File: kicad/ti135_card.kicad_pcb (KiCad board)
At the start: 8 copper layers, 76 x 65.1 mm, 302 parts, among them J1 JTAG 3.3V, J2 UART 3.3V, J3 2x19 1.27mm socket (bottom), J5 LCD 1x14 2.54mm, J6 2x3 1.27mm (bottom), J9 HR911130A, U1001 THGAMVG7T13BAIL, U101 NCP163ASN330T1G, U1201 SN74AXC8T245PWR, U1202 SN74AXC8T245PWR, U1203 SN74AXC8T245PWR, U1204 SN74AXC8T245PWR, U1301 SN74LV4051APWR, U1302 OPA365AIDBVR, U1303 ADS7056IRUGR, U201 TLV62585PDRLR, U301 TLV62585PDRLR, U311 TLV62585PDRLR, U321 TLV62585PDRLR, U331 TLV62585PDRLR, U341 TLV62585PDRLR, U401 TPS3808G01DBVR, U501 Ti135N484I3, U601 IS25WP128-RHLE, U801 H9HCNNN8KUMLHR-NME, U901 KSZ9031RNXCA, U902 74LVC1G06GW, Y701 SiT8924BA-73-18N-25.000000, Y901 25MHz

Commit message: Placement with KiCadRoutingTools; Ethernet PHY changed to RTL8211FDI-CG
- Sheet 09 redone for the RTL8211FDI-CG (C692886; the KSZ9031 had 16 orderable, and the
  Agilex 5 card makes the same change). It runs from 3V3 only, with an internal 1.0 V core LDO
  and RGMII pads at 1.8 V from its pad LDO; all nine straps are fitted. PHYRSTB is a 3.3 V
  input, so it is driven through a 74LVC1G07 open drain. The jack LED is driven straight
  from LED2.
- The 1V2 buck (U321) is removed. Power budget and docs updated.
- make_board sets pad pin functions/types, so the placer reads the Y701 oscillator correctly.
- Placement: placement/ holds the inputs (groups, prep, intent fixes, judging chain). Seed 1
  of 12 was chosen by the quick-route judge and applied with tools/apply_placement.py.
  build_pcb.sh no longer rebuilds by default; --rebuild restores the poses.
- tools/jlc: the jlc-tools submodule.

Co-Authored-By: Claude Opus 5.5 <noreply@anthropic.com>
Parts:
- removed C321: 10u, Capacitor_SMD:C_0805_2012Metric
- removed C322, C923: 22u, Capacitor_SMD:C_0805_2012Metric
- removed C924, C942, C943: 100n, Capacitor_SMD:C_0402_1005Metric
- removed FB902: BLM15PX121SN1D, Inductor_SMD:L_0402_1005Metric
- removed L321: 1u, Inductor_SMD:L_Coilcraft_XxL4020
- removed R321, R322: 100k, Resistor_SMD:R_0402_1005Metric
- removed U321: TLV62585PDRLR, Package_TO_SOT_SMD:SOT-563
- added R932: 10k, Resistor_SMD:R_0402_1005Metric, F.Cu at (191.7, 73.9)
- added R933: 10k, Resistor_SMD:R_0402_1005Metric, F.Cu at (184.7, 72.8)
- C509, C510, C511, C512, C513, C514, C515, C516, C517, C518, C519, C520, C521, C522, C523, C524, C525, C526, C527, C528, C529, C530, C531, C532, C533, C534, C535, C536, C537, C538, C539, C540, C541, C542, C543, C544, C545, C546, C547, C548, C549, C550, C551, C552, C553, C554, C555, C556, C557, C558, C559, C560, C561, C562, C563, C564, C565, C803, C804, C805, C806, C807, C808, C809, C810, C811, C812, C813, C814, C815, C816, C817, C818, C819, C820, C821, C822, C823, C824, C825, C826, C827, C828, C829, C830, C831, C832, C833, C834, C835: moved to B.Cu
- C920: value 22u -> 10u
- C930: value 10u -> 1u; footprint Capacitor_SMD:C_0805_2012Metric -> Capacitor_SMD:C_0402_1005Metric
- C935: value 100n -> 1u
- C940: value 4u7 -> 1u
- R928, R929: value 1k -> 4k7
- R930: value 10k -> 4k7
- R931: value 12.1k 1% -> 2.49k 1%
- U901: value KSZ9031RNXCA -> RTL8211FDI-CG; footprint Package_DFN_QFN:QFN-48-1EP_7x7mm_P0.5mm_EP5.15x5.15mm -> Package_DFN_QFN:QFN-40-1EP_5x5mm_P0.4mm_EP3.6x3.6mm_ThermalVias
- U902: value 74LVC1G06GW -> 74LVC1G07GW
- moved C546 212.5 mm to (161.7, 75.0)
- moved C542 203.1 mm to (157.6, 76.3), turned to -90 degrees
- moved C545 201.4 mm to (169.7, 69.8), turned to 90 degrees
- moved C543 200.2 mm to (163.8, 75.1), turned to -90 degrees
- moved R930 199.5 mm to (181.0, 80.9), turned to 180 degrees
- moved C544 195.7 mm to (171.6, 77.4), turned to 180 degrees
- moved R929 195.3 mm to (181.5, 82.4), turned to 90 degrees
- moved C539 190.8 mm to (159.8, 74.5), turned to 90 degrees
- moved C540 188.9 mm to (165.2, 74.2), turned to 90 degrees
- moved C541 188.3 mm to (169.1, 73.2), turned to 180 degrees
- moved RN1407 182.2 mm to (137.0, 56.1), turned to 180 degrees
- moved R801 180.3 mm to (158.9, 69.9), turned to 90 degrees
- moved RN1406 175.7 mm to (141.8, 57.9), turned to 180 degrees
- moved C537 174.8 mm to (167.6, 74.1), turned to -90 degrees
- moved R927 173.4 mm to (199.8, 75.5), turned to 90 degrees
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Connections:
- C901 pad 1: /eth_rst_n -> /09 ethernet/phy_rstb
- C920 pad 1: /09 ethernet/phy_avddh -> /09 ethernet/phy_avdd33
- C921 pad 1: /09 ethernet/phy_avddh -> /09 ethernet/phy_avdd33
- C922 pad 1: /09 ethernet/phy_avddh -> /09 ethernet/phy_avdd33
- C930 pad 1: 1V2 -> /09 ethernet/phy_vdd10
- C931 pad 1: 1V2 -> /09 ethernet/phy_vdd10
- C932 pad 1: 1V2 -> /09 ethernet/phy_vdd10
- C933 pad 1: 1V2 -> /09 ethernet/phy_vdd10
- C934 pad 1: 1V2 -> /09 ethernet/phy_vdd10
- C935 pad 1: 1V2 -> /09 ethernet/phy_dvdd_rg
- C936 pad 1: 1V2 -> /09 ethernet/phy_dvdd_rg
- C940 pad 1: 1V8 -> 3V3
- C941 pad 1: 1V8 -> 3V3
- FB901 pad 2: /09 ethernet/phy_avddh -> /09 ethernet/phy_avdd33
- R920 pad 1: 1V8 -> /09 ethernet/phy_dvdd_rg
- R920 pad 2: /rgmii_rxd0 -> /09 ethernet/phy_rxd3
- R921 pad 1: 1V8 -> /09 ethernet/phy_rxc
- R921 pad 2: /rgmii_rxd1 -> GND
- R922 pad 1: 1V8 -> /09 ethernet/phy_rx_ctl
- R922 pad 2: /rgmii_rxd2 -> GND
- R923 pad 1: 1V8 -> /09 ethernet/phy_rxd2
- R923 pad 2: /rgmii_rxd3 -> GND
- R924 pad 1: 1V8 -> /09 ethernet/phy_rxd1
- R924 pad 2: /09 ethernet/phy_led_mode -> GND
- R925 pad 1: 1V8 -> /09 ethernet/phy_dvdd_rg
- R925 pad 2: /eth_mdio -> /09 ethernet/phy_rxd0
- R926 pad 1: 1V8 -> /09 ethernet/phy_led0
- R926 pad 2: /eth_mdc -> GND
- R927 pad 1: 1V8 -> /09 ethernet/phy_led1
- R927 pad 2: /eth_int_n -> GND
- R928 pad 1: /09 ethernet/phy_led2 -> 3V3
- R928 pad 2: GND -> /09 ethernet/eth_led_k
- R929 pad 1: /09 ethernet/phy_led1 -> 1V8
- R929 pad 2: GND -> /eth_mdio
- R930 pad 1: /eth_rst_n -> 1V8
- R930 pad 2: GND -> /eth_int_n
- R931 pad 1: /09 ethernet/phy_iset -> /09 ethernet/phy_rset
- U901 pad 1: /09 ethernet/phy_avddh -> /09 ethernet/eth_mdi_a_P
- U901 pad 10: /09 ethernet/eth_mdi_d_P -> /09 ethernet/eth_mdi_d_N
- U901 pad 11: /09 ethernet/eth_mdi_d_N -> /09 ethernet/phy_avdd33
- U901 pad 12: /09 ethernet/phy_avddh -> /09 ethernet/phy_rstb
- U901 pad 13: unconnected-(U901-NC-Pad13) -> /eth_mdc
- U901 pad 14: 1V2 -> /eth_mdio
- U901 pad 15: /09 ethernet/phy_led2 -> /09 ethernet/phy_txd3
- U901 pad 16: 1V8 -> /09 ethernet/phy_txd2
- U901 pad 17: /09 ethernet/phy_led1 -> /09 ethernet/phy_txd1
- U901 pad 18: 1V2 -> /09 ethernet/phy_txd0
- U901 pad 19: /09 ethernet/phy_txd0 -> /09 ethernet/phy_tx_ctl
- U901 pad 2: /09 ethernet/eth_mdi_a_P -> /09 ethernet/eth_mdi_a_N
- U901 pad 20: /09 ethernet/phy_txd1 -> /09 ethernet/phy_txc
- U901 pad 21: /09 ethernet/phy_txd2 -> /09 ethernet/phy_vdd10
- U901 pad 22: /09 ethernet/phy_txd3 -> /09 ethernet/phy_rxd3
- U901 pad 23: 1V2 -> /09 ethernet/phy_rxd2
- U901 pad 24: /09 ethernet/phy_txc -> /09 ethernet/phy_rxd1
- U901 pad 25: /09 ethernet/phy_tx_ctl -> /09 ethernet/phy_rxd0
- U901 pad 26: 1V2 -> /09 ethernet/phy_rx_ctl
- U901 pad 27: /09 ethernet/phy_rxd3 -> /09 ethernet/phy_rxc
- U901 pad 28: /09 ethernet/phy_rxd2 -> /09 ethernet/phy_dvdd_rg
- U901 pad 29: GND -> 3V3
- U901 pad 3: /09 ethernet/eth_mdi_a_N -> /09 ethernet/phy_vdd10
- U901 pad 30: 1V2 -> /09 ethernet/phy_vdd10
- U901 pad 31: /09 ethernet/phy_rxd1 -> /eth_int_n
- U901 pad 32: /09 ethernet/phy_rxd0 -> /09 ethernet/phy_led0
- U901 pad 33: /09 ethernet/phy_rx_ctl -> /09 ethernet/phy_led1
- U901 pad 34: 1V8 -> /09 ethernet/eth_led_k
- U901 pad 35: /09 ethernet/phy_rxc -> unconnected-(U901-CLKOUT-Pad35)
- U901 pad 36: /eth_mdc -> /09 ethernet/phy_xi
- U901 pad 37: /eth_mdio -> /09 ethernet/phy_xo
- U901 pad 38: /eth_int_n -> /09 ethernet/phy_vdd10
- U901 pad 39: 1V2 -> /09 ethernet/phy_rset
- U901 pad 4: 1V2 -> /09 ethernet/eth_mdi_b_P
- U901 pad 40: 1V8 -> /09 ethernet/phy_avdd33
- U901 pad 41: /09 ethernet/phy_led_mode -> GND
- U901 pad 5: /09 ethernet/eth_mdi_b_P -> /09 ethernet/eth_mdi_b_N
- U901 pad 6: /09 ethernet/eth_mdi_b_N -> /09 ethernet/eth_mdi_c_P
- U901 pad 7: /09 ethernet/eth_mdi_c_P -> /09 ethernet/eth_mdi_c_N
- U901 pad 8: /09 ethernet/eth_mdi_c_N -> /09 ethernet/phy_vdd10
- U901 pad 9: 1V2 -> /09 ethernet/eth_mdi_d_P
- U902 pad 1: (no net) -> unconnected-(U902-NC-Pad1)
- U902 pad 2: /09 ethernet/phy_led1 -> /eth_rst_n
- U902 pad 4: /09 ethernet/eth_led_k -> /09 ethernet/phy_rstb

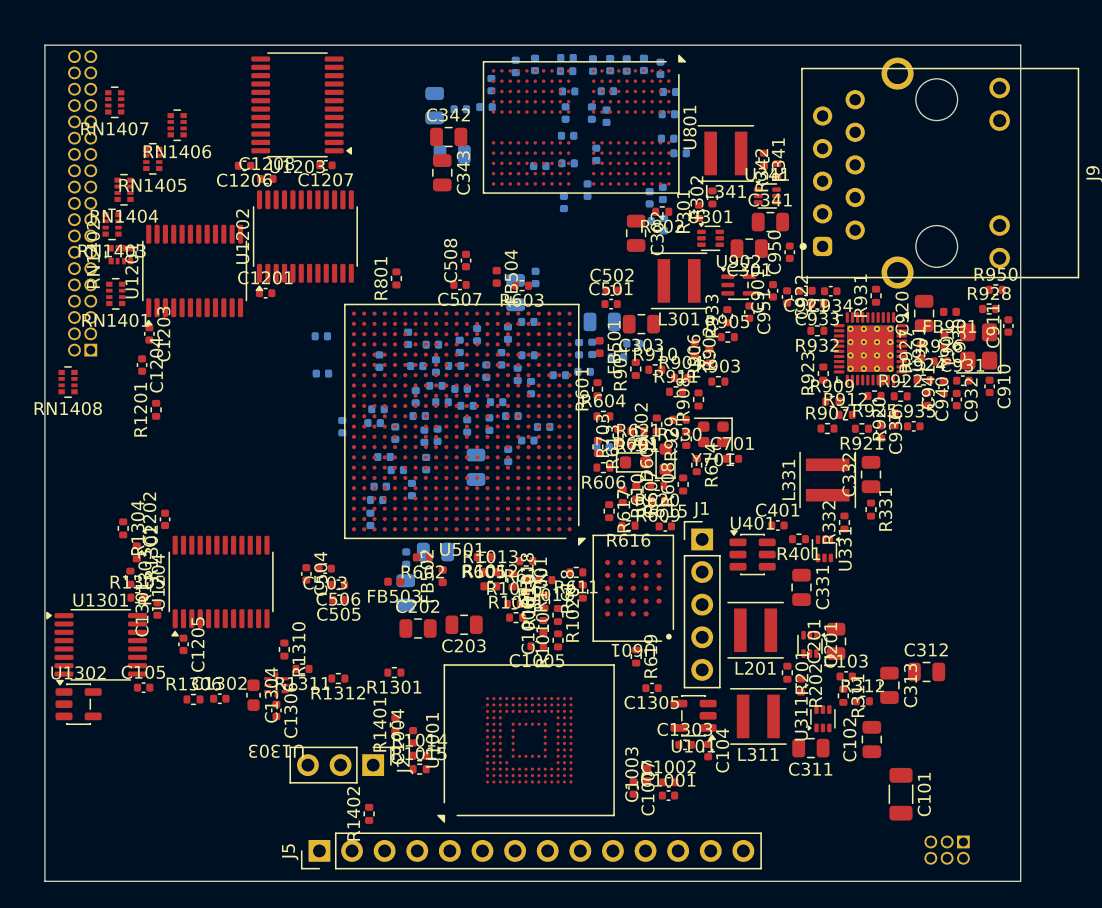
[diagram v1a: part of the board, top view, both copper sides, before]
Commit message: Placement with power on the underside; LPDDR4 swizzle, 40/80 ohm rules, layer and plane plan
- LPDDR4 DQ swizzle within each byte (crossings 125 -> 45). efinity/pinplan/lpddr4_swizzle.json
  is the one source for the schematic (sheet 08) and the Interface Designer PIN_SWIZZLE_DQM*
  (read back and checked). Write-up in LPDDR4_SWIZZLE.md; scorer in tools/lpddr4_swizzle_score.py.
- Stack-up: a field solve (tools/zsolve.py) of JLC08161H-3313. Layer roles are now In1/In6 GND and
  In3/In4 planes, with signals on F/In2/In5/B. LPDDR4 widths follow the Efinix 40 ohm / 80 ohm
  guide (0.18 mm and 0.14/0.15 mm on In2/In5). Plane plan in TI135_PCB_NOTES.md section 6.6
  (KiCadRoutingTools recommend-stackup / recommend-plane-mappings).
- Ti135N484I3 LPDDR4 limit recorded: 2.8 Gbps (data sheet Table 22). Card-to-baseboard gap
  about 5.3 mm, so the power supplies go on the underside, as on the Ti60 card.
- Placement: the five TLV62585 cells are held to TI's Figure 24 layout (placement/sketches) and
  placed on B.Cu with J6's caps. J1/J2 are moved to the west edge, over an empty baseboard area.
  Seed 8 of 12 was applied: its quick route left 24 nets open, against 34 and 38 for the next
  seeds.
- LAYOUT_PLAN.md: the placement and routing plan, with the tool for each step.

Co-Authored-By: Claude Opus 5.5 <noreply@anthropic.com>
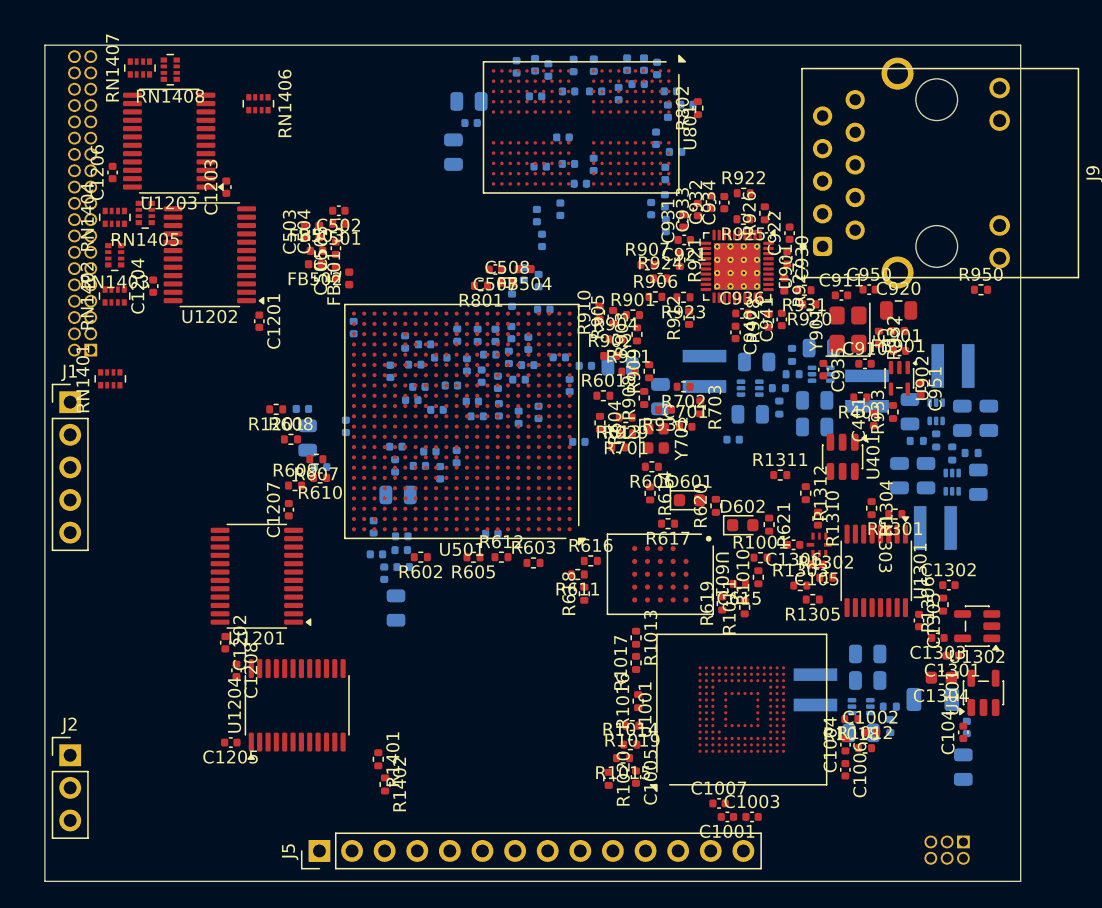
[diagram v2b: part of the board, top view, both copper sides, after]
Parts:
- C101, C102, C103, C201, C202, C203, C301, C302, C303, C311, C312, C313, C331, C332, C341, C342, C343, L201, L301, L311, L331, L341, R201, R202, R301, R302, R311, R312, R331, R332, R341, R342, U201, U301, U311, U331, U341: moved to B.Cu
- moved U1302 70.3 mm to (204.1, 96.9), turned to 180 degrees
- moved C1301 62.0 mm to (202.2, 99.2), turned to 180 degrees
- moved U1301 60.7 mm to (196.3, 92.6), turned to -90 degrees
- moved R1306 58.8 mm to (201.5, 95.3), turned to 90 degrees
- moved R1304 58.3 mm to (195.9, 87.8)
- moved C1302 57.5 mm to (201.9, 93.8)
- moved R1302 53.7 mm to (192.4, 93.2), turned to 0 degrees
- moved C1304 53.6 mm to (201.4, 101.0), turned to 180 degrees
- moved C105 53.3 mm to (191.7, 92.1), turned to 180 degrees
- moved R1305 52.6 mm to (191.3, 94.9), turned to 180 degrees
- moved R1303 52.2 mm to (190.4, 93.8), turned to 0 degrees
- moved J1 50.4 mm to (133.5, 79.5)
- moved U1303 49.4 mm to (196.5, 90.6), turned to -90 degrees
- moved R1310 42.8 mm to (191.7, 88.6)
- moved C1306 42.3 mm to (189.8, 90.6), turned to 180 degrees
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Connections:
- U801 pad AA11: /08 lpddr4/ddr_dq24 -> /08 lpddr4/ddr_dq28
- U801 pad AA2: /08 lpddr4/ddr_dq16 -> /08 lpddr4/ddr_dq19
- U801 pad AA4: /08 lpddr4/ddr_dq23 -> /08 lpddr4/ddr_dq18
- U801 pad AA9: /08 lpddr4/ddr_dq31 -> /08 lpddr4/ddr_dq25
- U801 pad B2: /08 lpddr4/ddr_dq0 -> /08 lpddr4/ddr_dq2
- U801 pad B4: /08 lpddr4/ddr_dq7 -> /08 lpddr4/ddr_dq1
- U801 pad B9: /08 lpddr4/ddr_dq15 -> /08 lpddr4/ddr_dq11
- U801 pad C2: /08 lpddr4/ddr_dq1 -> /08 lpddr4/ddr_dq5
- U801 pad C4: /08 lpddr4/ddr_dq6 -> /08 lpddr4/ddr_dq0
- U801 pad C9: /08 lpddr4/ddr_dq14 -> /08 lpddr4/ddr_dq10
- U801 pad E11: /08 lpddr4/ddr_dq10 -> /08 lpddr4/ddr_dq12
- U801 pad E2: /08 lpddr4/ddr_dq2 -> /08 lpddr4/ddr_dq7
- U801 pad E4: /08 lpddr4/ddr_dq5 -> /08 lpddr4/ddr_dq4
- U801 pad E9: /08 lpddr4/ddr_dq13 -> /08 lpddr4/ddr_dq14
- U801 pad F11: /08 lpddr4/ddr_dq11 -> /08 lpddr4/ddr_dq13
- U801 pad F2: /08 lpddr4/ddr_dq3 -> /08 lpddr4/ddr_dq6
- U801 pad F4: /08 lpddr4/ddr_dq4 -> /08 lpddr4/ddr_dq3
- U801 pad F9: /08 lpddr4/ddr_dq12 -> /08 lpddr4/ddr_dq15
- U801 pad U11: /08 lpddr4/ddr_dq27 -> /08 lpddr4/ddr_dq30
- U801 pad U2: /08 lpddr4/ddr_dq19 -> /08 lpddr4/ddr_dq17
- U801 pad U4: /08 lpddr4/ddr_dq20 -> /08 lpddr4/ddr_dq22
- U801 pad U9: /08 lpddr4/ddr_dq28 -> /08 lpddr4/ddr_dq27
- U801 pad V11: /08 lpddr4/ddr_dq26 -> /08 lpddr4/ddr_dq31
- U801 pad V2: /08 lpddr4/ddr_dq18 -> /08 lpddr4/ddr_dq21
- U801 pad V4: /08 lpddr4/ddr_dq21 -> /08 lpddr4/ddr_dq23
- U801 pad V9: /08 lpddr4/ddr_dq29 -> /08 lpddr4/ddr_dq24
- U801 pad Y11: /08 lpddr4/ddr_dq25 -> /08 lpddr4/ddr_dq29
- U801 pad Y2: /08 lpddr4/ddr_dq17 -> /08 lpddr4/ddr_dq20
- U801 pad Y4: /08 lpddr4/ddr_dq22 -> /08 lpddr4/ddr_dq16
- U801 pad Y9: /08 lpddr4/ddr_dq30 -> /08 lpddr4/ddr_dq26

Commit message: Hand touch-ups: RGMII resistors, PHY crystal, DDR_CAL/ZQ placed by proximity claims; labels tidied
The 60 parts around the PHY, the RGMII resistors and R801/R802 were re-placed with everything
else locked and proximity claims to their pads (work/touch, place_simple --claim-weight 20):
RX resistors within 1.5 mm of the PHY, Y901 2 mm from XTAL_IN, R801/R802 about 3 mm from
DDR_CAL/ZQ. Reference labels tidied with beautify_labels (175 at 1.0 mm); 92 that have no
legal spot are hidden. apply_placement.py gains --keep-locks.

Co-Authored-By: Claude Opus 5.5 <noreply@anthropic.com>
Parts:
- moved C505 39.3 mm to (161.0, 106.2), turned to 0 degrees
- moved C504 37.6 mm to (174.9, 96.7), turned to 0 degrees
- moved C506 37.1 mm to (159.1, 106.2), turned to 180 degrees
- moved C503 36.8 mm to (174.6, 95.1)
- moved FB503 28.4 mm to (160.4, 95.1)
- moved FB502 28.4 mm to (161.9, 95.6), turned to -90 degrees
- moved R933 16.0 mm to (182.1, 76.5)
- moved C935 15.5 mm to (178.2, 70.3), turned to 180 degrees
- moved C921 14.9 mm to (195.4, 71.8), turned to 0 degrees
- moved R921 14.1 mm to (193.8, 74.3), turned to 0 degrees
- moved R926 12.3 mm to (193.8, 75.3), turned to 0 degrees
- moved R928 11.7 mm to (199.5, 72.0), turned to 180 degrees
- moved R908 10.3 mm to (186.2, 72.6), turned to 180 degrees
- moved R907 10.2 mm to (187.7, 73.1), turned to 90 degrees
- moved R910 9.90 mm to (184.6, 73.1)
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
